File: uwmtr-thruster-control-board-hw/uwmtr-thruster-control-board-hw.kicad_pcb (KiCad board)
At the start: 4 copper layers, 40 x 49.2 mm, 17 parts, among them J1 Conn_01x13_Pin, J2 691137710003, J3 691137710002, U1 TI_MCF8316A

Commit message: Switching resistors to JLCPCB assembly non-extended parts.
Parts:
- removed 1206W4F5101T5E1, 1206W4F5101T5E2, 1206W4F5101T5E3, 1206W4F5101T5E4: 5.1kR, Resistor_SMD:R_1206_3216Metric
- added R2: 5.1KΩ, Resistor_SMD:R_0603_1608Metric, F.Cu at (150.8, 104.1)
- added R3: 5.1KΩ, Resistor_SMD:R_0603_1608Metric, F.Cu at (162.9, 116.2)
- added R4: 5.1KΩ, Resistor_SMD:R_0603_1608Metric, F.Cu at (151.8, 114.7)
- added R5: 5.1KΩ, Resistor_SMD:R_0603_1608Metric, F.Cu at (148.2, 114.7)
- R1: footprint Resistor_THT:R_Axial_DIN0207_L6.3mm_D2.5mm_P10.16mm_Horizontal -> Resistor_SMD:R_1206_3216Metric
- moved R1 5.47 mm to (176.4, 113.2)
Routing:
- net /AVDD: track 45.0 -> 42.4 mm
- net /FG: track 43.3 -> 41.8 mm
- net /SW_BK: vias 0 -> 3
- net +3.3V: vias 0 -> 3

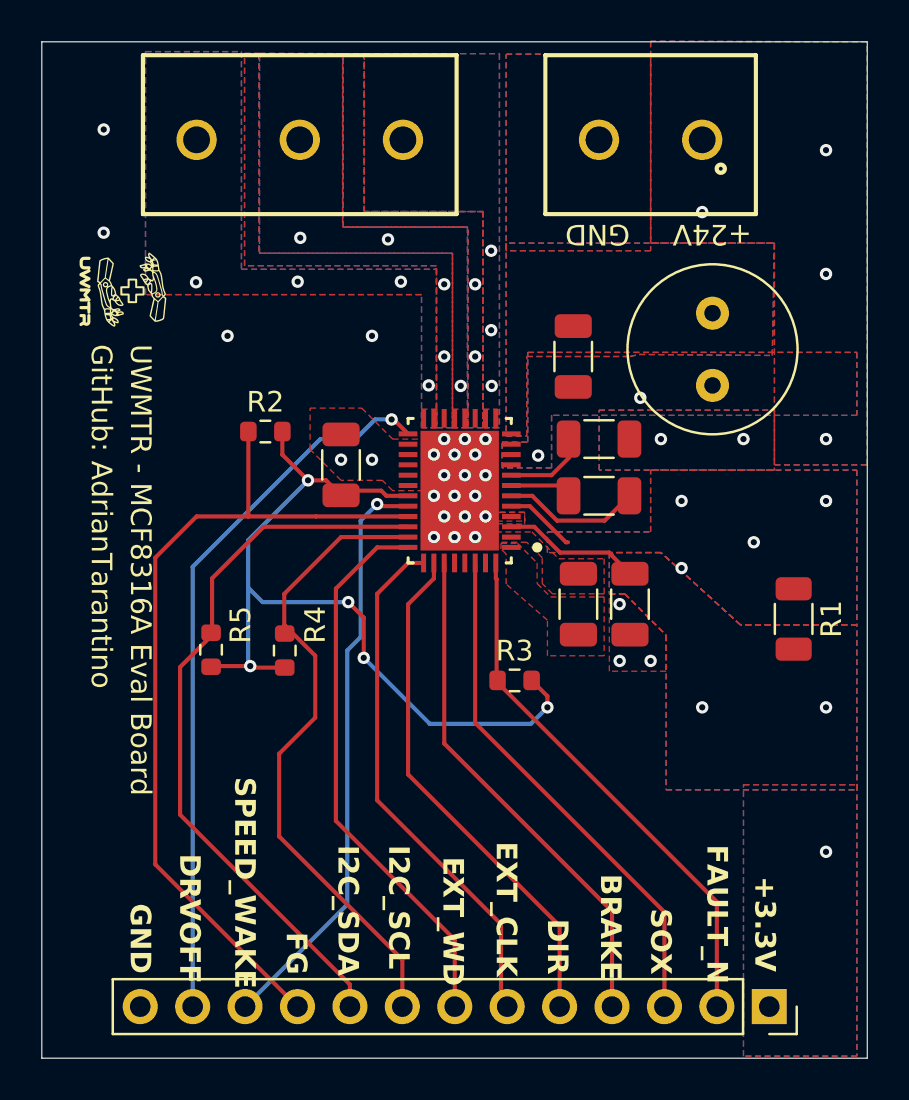
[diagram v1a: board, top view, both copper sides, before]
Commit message: Switching components to non-extended library components where applicable and adding labels.
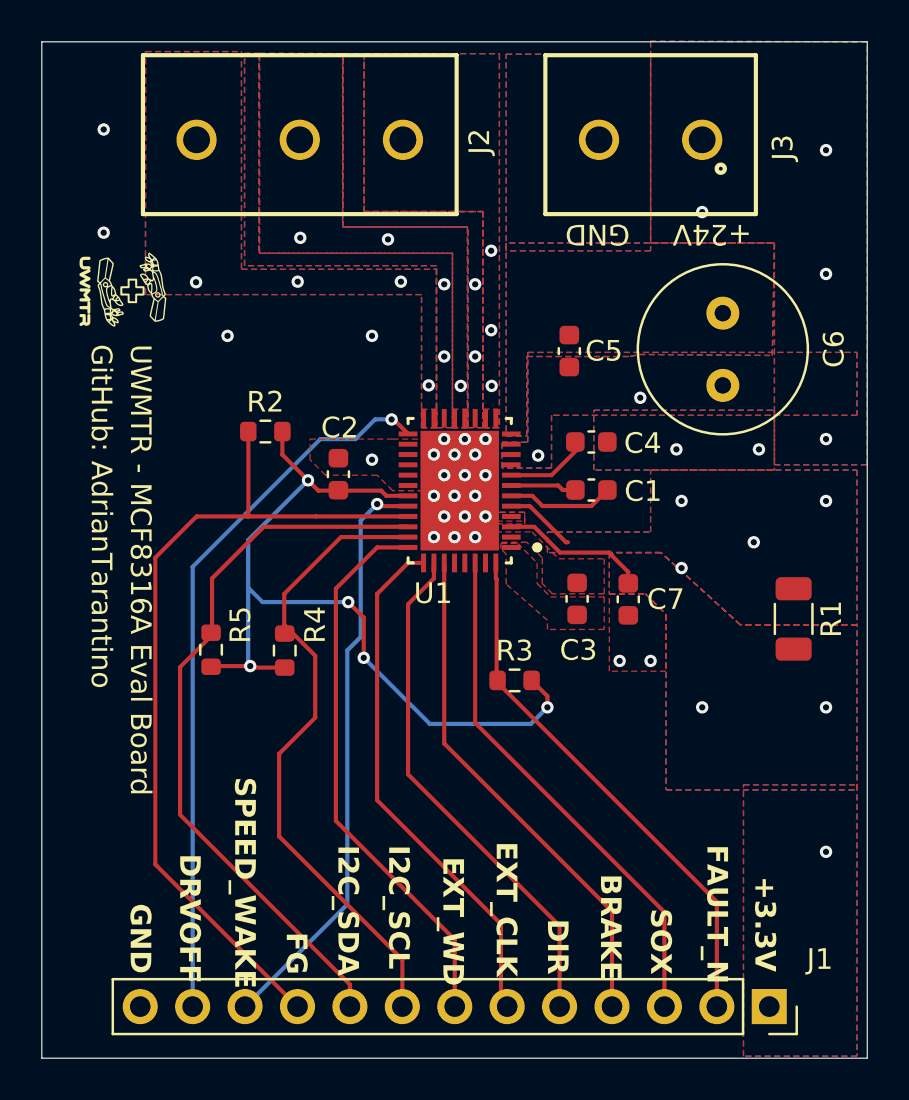
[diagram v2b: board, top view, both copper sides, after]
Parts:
- removed 1206B473K500NT1: 47nF, Capacitor_SMD:C_1206_3216Metric
- removed CL31B104KCFNNNE1: 100nF, Capacitor_SMD:C_1206_3216Metric
- removed CL31B105KAHNNNE1, CL31B105KAHNNNE2, CL31B105KAHNNNE3: 1uF, Capacitor_SMD:C_1206_3216Metric
- removed CS3216X5R226K160NRI1: 22uF, Capacitor_SMD:C_1206_3216Metric
- added C1: 47nF, Capacitor_SMD:C_0603_1608Metric, F.Cu at (166.6, 107.0)
- added C2: 1uF, Capacitor_SMD:C_0603_1608Metric, F.Cu at (154.4, 106.2)
- added C3: 1uF, Capacitor_SMD:C_0603_1608Metric, F.Cu at (165.9, 112.2)
- added C4: 1uF, Capacitor_SMD:C_0603_1608Metric, F.Cu at (166.6, 104.6)
- added C5: 100nF, Capacitor_SMD:C_0603_1608Metric, F.Cu at (165.6, 100.2)
- added C7: 22uF, Capacitor_SMD:C_0603_1608Metric, F.Cu at (168.4, 112.3)
- moved C6 0.50 mm to (173.0, 101.9)
- renumbered KM107M050F12RR0VH2FP1 to C6
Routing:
- net /CPL: track 6.72 -> 5.18 mm
- net +3.3V: track 6.70 -> 7.39 mm
- net AGND: vias 24 -> 22
